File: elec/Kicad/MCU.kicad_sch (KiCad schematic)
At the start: 24 parts, among them J6 SWD, U1 STM32L053C8T6, Y1 32MHz, Y2 32.768KHz

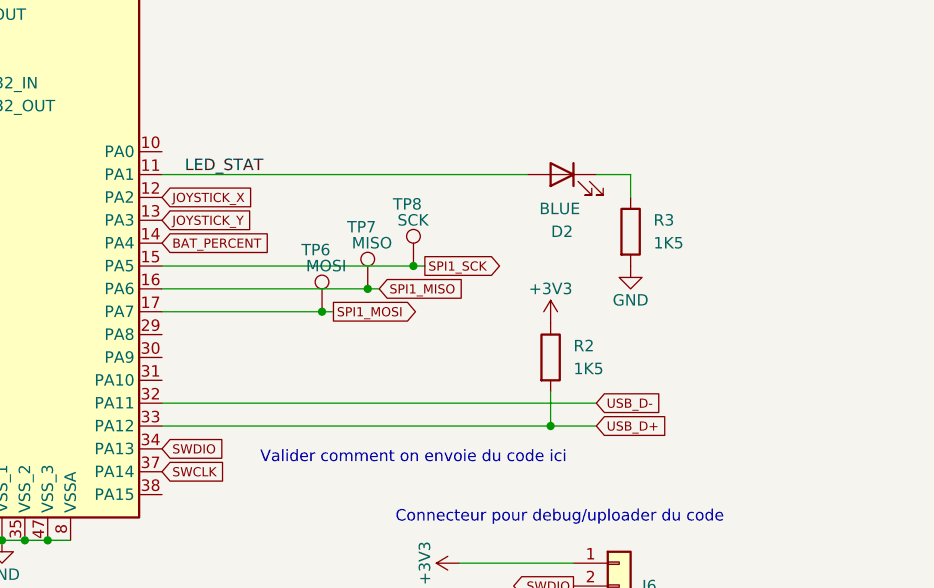
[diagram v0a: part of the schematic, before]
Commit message: add a solder jumper on USB_D+ line in case we need it
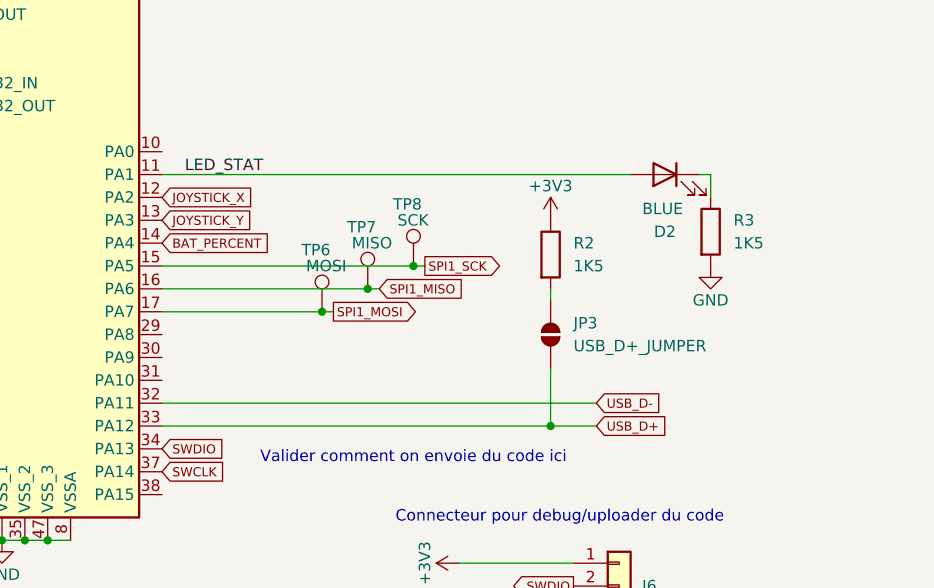
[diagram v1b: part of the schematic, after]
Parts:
- added JP3: USB_D+_JUMPER, symbol Jumper:SolderJumper_2_Open
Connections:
- net USB_D+: now also JP3.1 (A); no longer R2.2
- new net: JP3.2 (B), R2.2
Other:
- moved on the sheet: D2, R2, R3
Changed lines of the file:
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@@
 	(wire
 		(pts
-			(xy 156.21 129.54) (xy 156.21 125.73)
+			(xy 156.21 129.54) (xy 156.21 123.19)
 		)
 		(stroke
@@
 	(wire
 		(pts
-			(xy 161.29 101.6) (xy 165.1 101.6)
+			(xy 172.72 101.6) (xy 173.99 101.6)
 		)
 		(stroke
@@
 	(wire
 		(pts
-			(xy 113.03 101.6) (xy 153.67 101.6)
+			(xy 113.03 101.6) (xy 165.1 101.6)
 		)
 		(stroke
@@
 	(wire
 		(pts
-			(xy 165.1 101.6) (xy 165.1 104.14)
+			(xy 173.99 101.6) (xy 173.99 104.14)
 		)
 		(stroke
@@
 	(wire
 		(pts
+			(xy 156.21 115.57) (xy 156.21 114.3)
+		)
+		(stroke
+			(width 0)
+			(type default)
+		)
+	)
+	(wire
+		(pts
 			(xy 146.05 144.78) (xy 158.75 144.78)
 		)
@@
 	(symbol
 		(lib_id "Device:R")
-		(at 156.21 121.92 0)
+		(at 156.21 110.49 0)
 		(unit 1)
 		(exclude_from_sim no)
@@
 		(fields_autoplaced yes)
 		(property "Reference" "R2"
-			(at 158.75 120.6499 0)
+			(at 158.75 109.2199 0)
 			(effects
 				(font
@@
 		)
 		(property "Value" "1K5"
-			(at 158.75 123.1899 0)
+			(at 158.75 111.7599 0)
 			(effects
 				(font
@@
 		)
 		(property "Footprint" ""
-			(at 154.432 121.92 90)
+			(at 154.432 110.49 90)
 			(effects
 				(font
@@
 		)
 		(property "Datasheet" "https://www.digikey.ca/en/products/detail/vishay-dale/CRCW04021M00FKED/1178349"
-			(at 156.21 121.92 0)
+			(at 156.21 110.49 0)
 			(effects
 				(font
@@
 		)
 		(property "Description" ""
-			(at 156.21 121.92 0)
+			(at 156.21 110.49 0)
 			(effects
 				(font
@@
 	(symbol
 		(lib_id "Device:R")
-		(at 165.1 107.95 0)
+		(at 173.99 107.95 0)
 		(unit 1)
 		(exclude_from_sim no)
@@
 		(fields_autoplaced yes)
 		(property "Reference" "R3"
-			(at 167.64 106.6799 0)
+			(at 176.53 106.6799 0)
 			(effects
 				(font
@@
 		)
 		(property "Value" "1K5"
-			(at 167.64 109.2199 0)
+			(at 176.53 109.2199 0)
 			(effects
 				(font
@@
 		)
 		(property "Footprint" ""
-			(at 163.322 107.95 90)
+			(at 172.212 107.95 90)
 			(effects
 				(font
@@
 		)
 		(property "Datasheet" "https://www.digikey.ca/en/products/detail/yageo/RC0603FR-07510KL/727286"
-			(at 165.1 107.95 0)
+			(at 173.99 107.95 0)
 			(effects
 				(font
@@
 		)
 		(property "Description" ""
-			(at 165.1 107.95 0)
+			(at 173.99 107.95 0)
 			(effects
 				(font
@@
 	(symbol
 		(lib_id "Device:LED")
-		(at 157.48 101.6 0)
+		(at 168.91 101.6 0)
 		(mirror y)
 		(unit 1)
@@
 		(dnp no)
 		(property "Reference" "D2"
-			(at 157.48 107.95 0)
+			(at 168.91 107.95 0)
 			(effects
 				(font
@@
 		)
 		(property "Value" "BLUE"
-			(at 157.226 105.41 0)
+			(at 168.656 105.41 0)
 			(effects
 				(font
@@
 		)
 		(property "Footprint" ""
-			(at 157.48 101.6 0)
+			(at 168.91 101.6 0)
 			(effects
 				(font
@@
 		)
 		(property "Datasheet" "~"
-			(at 157.48 101.6 0)
+			(at 168.91 101.6 0)
 			(effects
 				(font
@@
 		)
 		(property "Description" ""
-			(at 157.48 101.6 0)
+			(at 168.91 101.6 0)
 			(effects
 				(font
@@
 		(lib_name "GND_1")
 		(lib_id "power:GND")
-		(at 165.1 111.76 0)
+		(at 173.99 111.76 0)
 		(unit 1)
 		(exclude_from_sim no)
@@
 		(dnp no)
 		(property "Reference" "#PWR06"
-			(at 165.1 118.11 0)
+			(at 173.99 118.11 0)
 			(effects
 				(font
@@
 		)
 		(property "Value" "GND"
-			(at 165.1 115.57 0)
+			(at 173.99 115.57 0)
 			(effects
 				(font
@@
 		)
 		(property "Footprint" ""
-			(at 165.1 111.76 0)
+			(at 173.99 111.76 0)
 			(effects
 				(font
@@
 		)
 		(property "Datasheet" ""
-			(at 165.1 111.76 0)
+			(at 173.99 111.76 0)
 			(effects
 				(font
@@
 		)
 		(property "Description" "Power symbol creates a global label with name \"GND\" , ground"
-			(at 165.1 111.76 0)
+			(at 173.99 111.76 0)
 			(effects
 				(font
@@
 	)
 	(symbol
+		(lib_id "Jumper:SolderJumper_2_Open")
+		(at 156.21 119.38 90)
+		(unit 1)
+		(exclude_from_sim yes)
+		(in_bom no)
+		(on_board yes)
+		(dnp no)
+		(fields_autoplaced yes)
+		(property "Reference" "JP3"
+			(at 158.75 118.1099 90)
+			(effects
+				(font
+					(size 1.27 1.27)
+				)
+				(justify right)
+			)
+		)
+		(property "Value" "USB_D+_JUMPER"
+			(at 158.75 120.6499 90)
+			(effects
+				(font
+					(size 1.27 1.27)
+				)
+				(justify right)
+			)
+		)
+		(property "Footprint" ""
+			(at 156.21 119.38 0)
+			(effects
+				(font
+					(size 1.27 1.27)
+				)
+				(hide yes)
+			)
+		)
+		(property "Datasheet" "~"
+			(at 156.21 119.38 0)
+			(effects
+				(font
+					(size 1.27 1.27)
+				)
+				(hide yes)
+			)
+		)
+		(property "Description" "Solder Jumper, 2-pole, open"
+			(at 156.21 119.38 0)
+			(effects
+				(font
+					(size 1.27 1.27)
+				)
+				(hide yes)
+			)
+		)
+		(pin "1"
+		)
+		(pin "2"
+		)
+		(instances
+			(project ""
+				(path "/a1545928-1195-40b9-b3c4-78f837012afb/47f0fc71-ff78-496f-bb04-036a9aeaa71c"
+					(reference "JP3")
+					(unit 1)
+				)
+			)
+		)
+	)
+	(symbol
 		(lib_id "Device:R")
 		(at 30.48 55.88 0)
@@
 	(symbol
 		(lib_id "power:+3V3")
-		(at 156.21 118.11 0)
+		(at 156.21 106.68 0)
 		(unit 1)
 		(exclude_from_sim no)
@@
 		(dnp no)
 		(property "Reference" "#PWR04"
-			(at 156.21 121.92 0)
+			(at 156.21 110.49 0)
 			(effects
 				(font
@@
 		)
 		(property "Value" "+3V3"
-			(at 156.21 114.3 0)
+			(at 156.21 102.87 0)
 			(effects
 				(font
@@
 		)
 		(property "Footprint" ""
-			(at 156.21 118.11 0)
+			(at 156.21 106.68 0)
 			(effects
 				(font
@@
 		)
 		(property "Datasheet" ""
-			(at 156.21 118.11 0)
+			(at 156.21 106.68 0)
 			(effects
 				(font
@@
 		)
 		(property "Description" "Power symbol creates a global label with name \"+3V3\""
-			(at 156.21 118.11 0)
+			(at 156.21 106.68 0)
 			(effects
 				(font

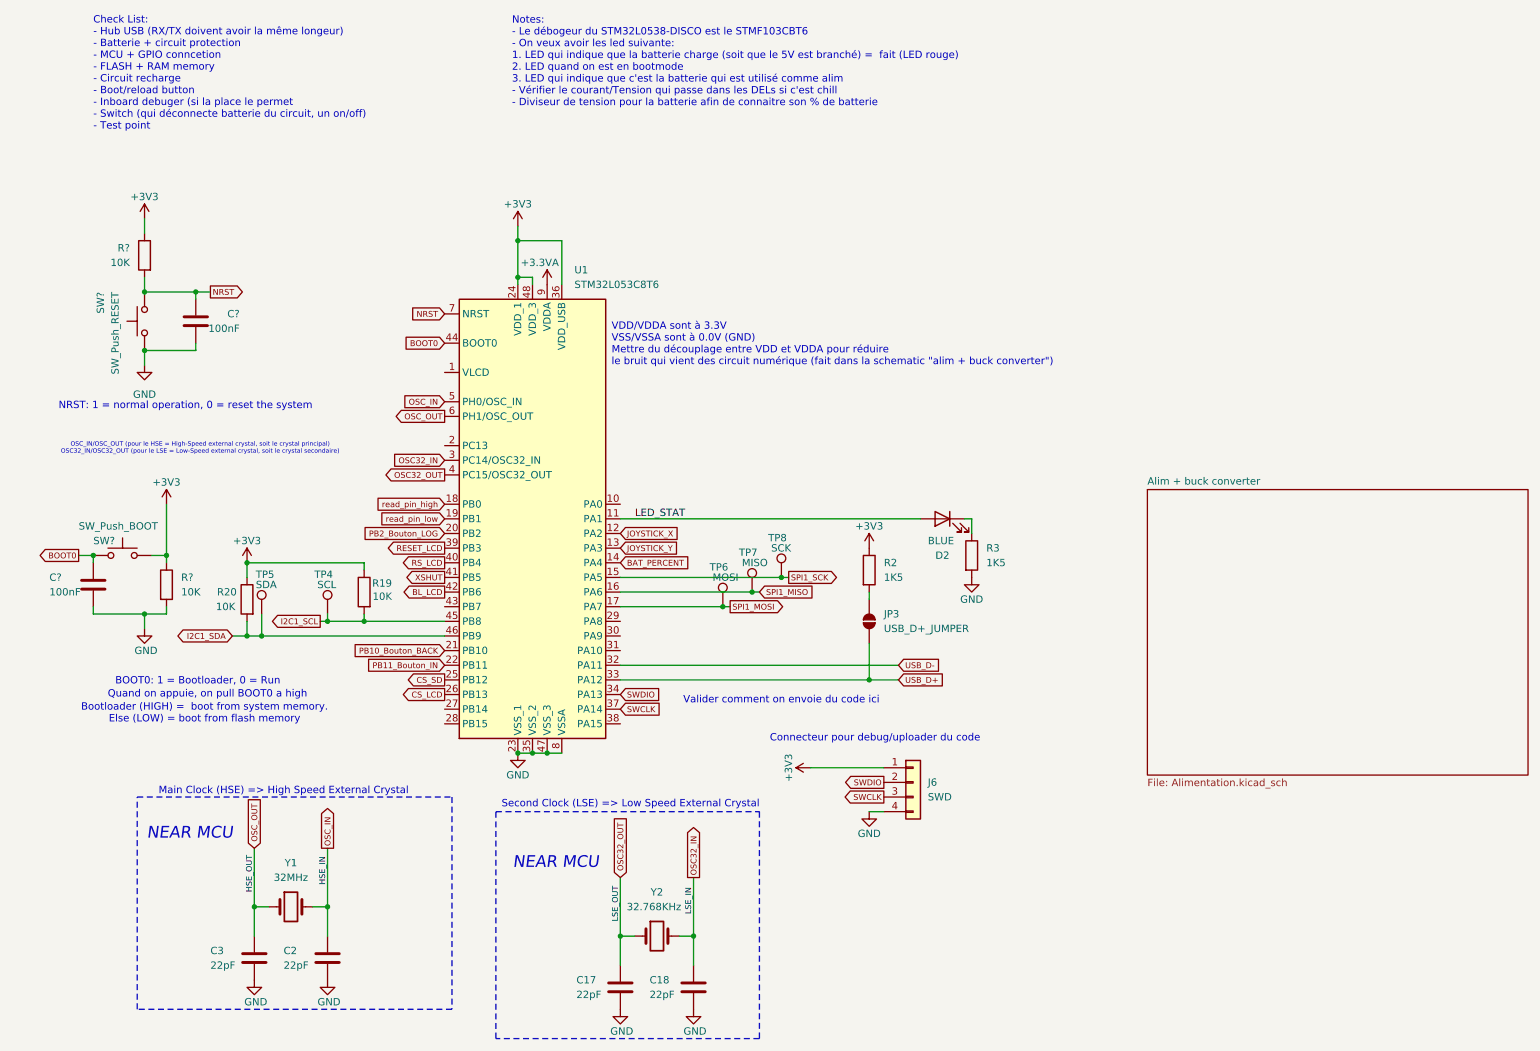
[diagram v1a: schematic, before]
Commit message: add a few footprint
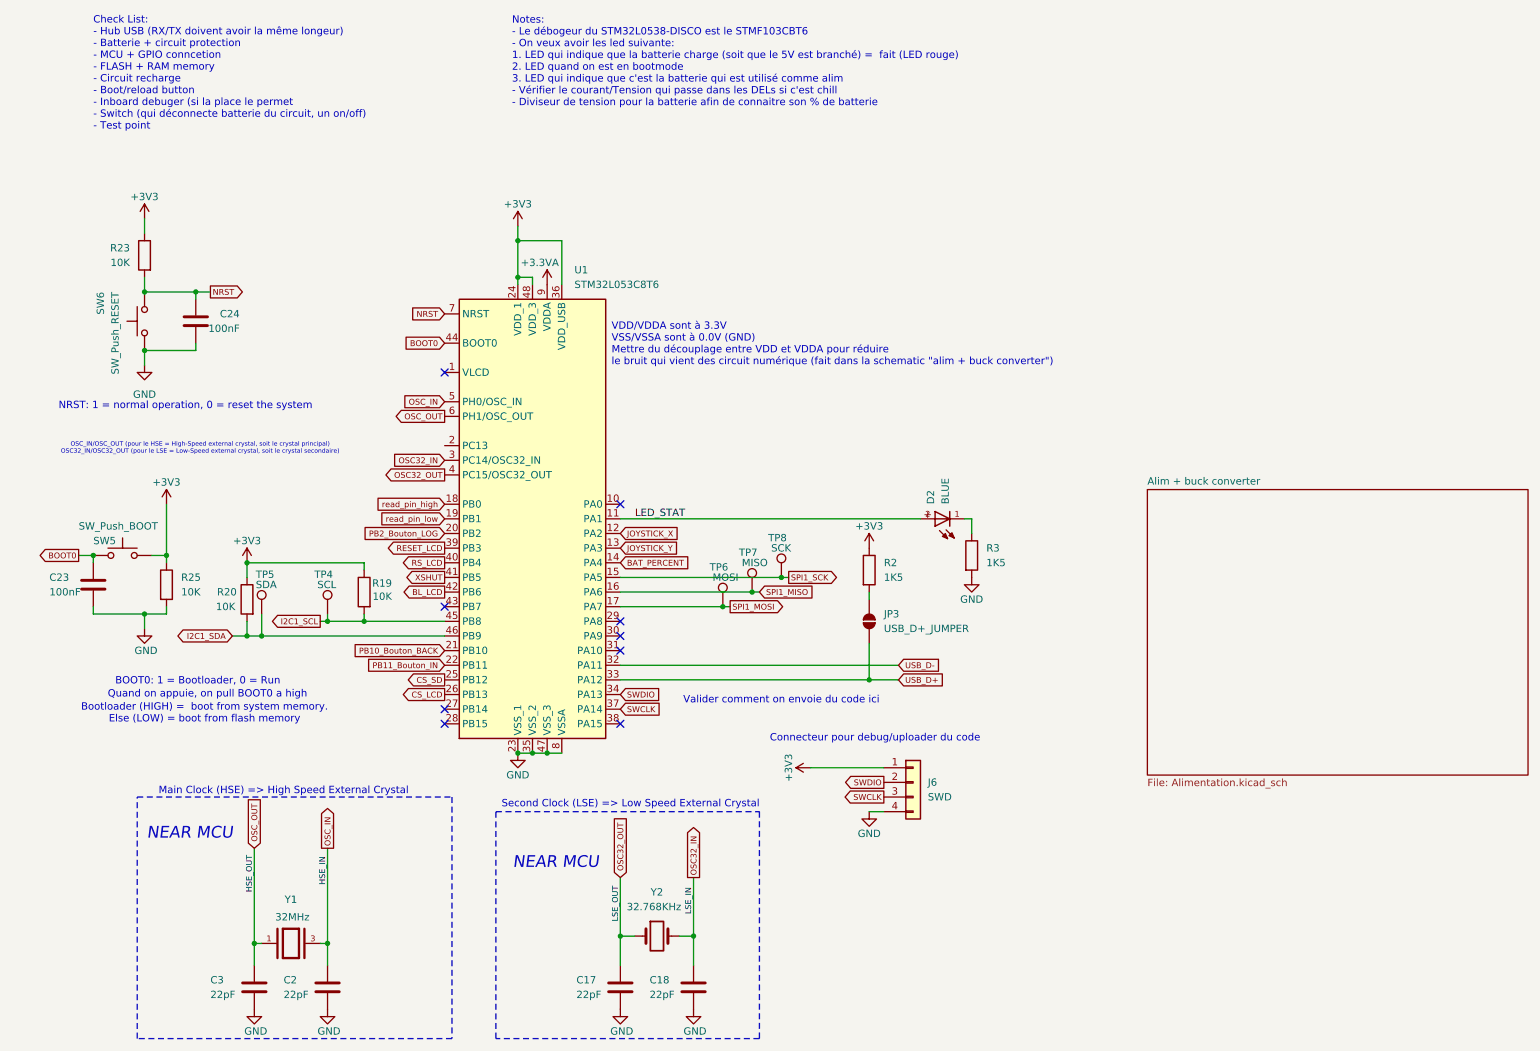
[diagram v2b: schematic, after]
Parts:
- removed D2: BLUE, symbol Device:LED
- removed Y1: 32MHz, symbol Device:Crystal
- added D2: BLUE, SMD_LED_0603:WL-SMCD_0603, symbol WL-SMCD_0603:WL-SMCD_0603
- added Y1: 32MHz, XRCGB32M000F2P01R0:OSC_XRCGB32M000F2P01R0, symbol XRCGB32M000F2P01R0:XRCGB32M000F2P01R0
- C17, C18, C2, C3: footprint (none) -> Capacitor_SMD:C_0603_1608Metric_Pad1.08x0.95mm_HandSolder
- C23, C24: renamed from C?; footprint (none) -> Capacitor_SMD:C_0603_1608Metric_Pad1.08x0.95mm_HandSolder
- J6: footprint Connector_PinHeader_1.00mm:PinHeader_1x04_P1.00mm_Vertical -> Connector_PinHeader_2.54mm:PinHeader_1x04_P2.54mm_Vertical
- JP3: footprint (none) -> Jumper:SolderJumper-2_P1.3mm_Open_TrianglePad1.0x1.5mm
- R19, R2, R20, R3: footprint (none) -> Resistor_SMD:R_0603_1608Metric_Pad0.98x0.95mm_HandSolder
- R23, R25: renamed from R?; footprint (none) -> Resistor_SMD:R_0603_1608Metric_Pad0.98x0.95mm_HandSolder
- SW5, SW6: renamed from SW?; footprint (none) -> Button_Switch_SMD:SW_SPST_PTS647_Sx38
- TP4, TP5, TP6, TP7, TP8: footprint (none) -> TestPoint:TestPoint_Loop_D1.80mm_Drill1.0mm_Beaded
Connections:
- net LED_STAT: now also D2.2
- net OSC_IN: now also Y1.3
- net OSC_OUT: now also Y1.1
- net at R3.1: now also D2.1
- no-connect marks 0 -> 9
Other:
- moved on the sheet: C2, C3

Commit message: formation torture
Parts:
- added J1: SWD, Connector_PinHeader_2.54mm:PinHeader_1x04_P2.54mm_Vertical, symbol Connector_Generic:Conn_01x04
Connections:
- net +3V3: now also J1.1 (Pin_1); no longer R19.1, R2.1, R20.1, R23.1, R25.1, SW5.1, U1.24 (VDD_1), U1.36 (VDD_USB), U1.48 (VDD_3)
- net GND: now also J1.4 (Pin_4)
- net USART1_TX: now reaches U1.30 (PA9)
- net USART1_TX: now also J1.2 (Pin_2)
- net USART1_RX: now reaches U1.31 (PA10)
- net USART1_RX: now also J1.3 (Pin_3)
- new net +3.3V: R19.1, R2.1, R20.1, R23.1, R25.1, SW5.1, U1.24 (VDD_1), U1.36 (VDD_USB), U1.48 (VDD_3)
- no-connect marks 9 -> 8
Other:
- note added: "Connector"
- note added: "USART Connector"
- moved on the sheet: J6, JP3, R2

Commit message: J'ai ajouter des power Flag pour spécifier a Kicad que c'est chill (faut qu'il apprenne a ce géré quand même)
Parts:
- removed JP3: USB_D+_JUMPER, Jumper:SolderJumper-2_P1.3mm_Open_TrianglePad1.0x1.5mm, symbol Jumper:SolderJumper_2_Open
- removed R2: 1K5, Resistor_SMD:R_0603_1608Metric_Pad0.98x0.95mm_HandSolder, symbol Device:R

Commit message: ajout d'un Mosfet de type N pour pouvoir gérer le % de batterie (ADC)
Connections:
- net +3V3 is gone; now on net +3.3V: J1.1 (Pin_1), J6.1 (Pin_1)
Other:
- note added: "Check List: - Hub USB (RX/TX doivent avoir la même longeur) - MCU + GPIO conncetion - Test point"
- note added: "HSE_IN"
- note added: "HSE_OUT"
- note added: "LSE_IN"
- note added: "LSE_OUT"
- note added: "Notes: Finir la schematic de charles"
- note removed: "Check List: - Hub USB (RX/TX doivent avoir la même longeur) - Batterie + circuit protection - MCU + GPIO conncetion - FLASH + RAM memory - Circuit recharge - Boot/reload button - Inboard debuger (si la place le permet - Switch (qui déconnecte batterie du circuit, un on/off) - Test point"
- note removed: "Notes: - Le débogeur du STM32L0538-DISCO est le STMF103CBT6 - On veux avoir les led suivante: 1. LED qui indique que la batterie charge (soit que le 5V est branché) = fait (LED rouge) 2. LED quand on est en bootmode 3. LED qui indique que c'est la batterie qui est utilisé comme alim - Vérifier le courant/Tension qui passe dans les DELs si c'est chill - Diviseur de tension pour la batterie afin de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"

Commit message: commencer le PCB vite fait
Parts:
- removed TP4: SCL, TestPoint:TestPoint_Loop_D1.80mm_Drill1.0mm_Beaded, symbol Connector:TestPoint
- removed TP5: SDA, TestPoint:TestPoint_Loop_D1.80mm_Drill1.0mm_Beaded, symbol Connector:TestPoint
- removed TP6: MOSI, TestPoint:TestPoint_Loop_D1.80mm_Drill1.0mm_Beaded, symbol Connector:TestPoint
- removed TP7: MISO, TestPoint:TestPoint_Loop_D1.80mm_Drill1.0mm_Beaded, symbol Connector:TestPoint
- removed TP8: SCK, TestPoint:TestPoint_Loop_D1.80mm_Drill1.0mm_Beaded, symbol Connector:TestPoint
- added J5: TestPoint, Connector_PinSocket_2.54mm:PinSocket_1x10_P2.54mm_Vertical, symbol Connector_Generic:Conn_01x10
- J1: value SWD -> USART
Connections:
- net +3.3V: now also J5.2 (Pin_2)
- net BAT_PERCENT: now also J5.4 (Pin_4)
- net GND: now also J5.10 (Pin_10)
- net I2C1_SCL: now also J5.5 (Pin_5)
- net I2C1_SDA: now also J5.6 (Pin_6)
- net SPI1_MISO: now also J5.8 (Pin_8)
- net SPI1_MOSI: now also J5.9 (Pin_9)
- net SPI1_SCK: now also J5.7 (Pin_7)
- new net +2V8: J5.1 (Pin_1)
- new net +5V: J5.3 (Pin_3)

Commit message: touillerie
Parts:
- removed J1: USART, Connector_PinHeader_2.54mm:PinHeader_1x04_P2.54mm_Vertical, symbol Connector_Generic:Conn_01x04
- removed J6: SWD, Connector_PinHeader_2.54mm:PinHeader_1x04_P2.54mm_Vertical, symbol Connector_Generic:Conn_01x04
- removed SW5: SW_Push_BOOT, Button_Switch_SMD:SW_SPST_PTS647_Sx38, symbol Switch:SW_Push
- removed SW6: SW_Push_RESET, Button_Switch_SMD:SW_SPST_PTS647_Sx38, symbol Switch:SW_Push
- added J1: USART, Connector_PinHeader_2.54mm:PinHeader_1x02_P2.54mm_Vertical, symbol Connector_Generic:Conn_01x02
- added J6: SWD, Connector_PinHeader_2.54mm:PinHeader_1x02_P2.54mm_Vertical, symbol Connector_Generic:Conn_01x02
- added SW4: SW_Push_RESET, B3U_1100P:B3U-1100P_OMR, symbol B3U_1100P:B3U-1100P
- added SW5: SW_Push_BOOT, B3U_1100P:B3U-1100P_OMR, symbol B3U_1100P:B3U-1100P
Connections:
- net +3.3V: now also SW5.2
- net BOOT0: now also SW5.1
- net GND: now also SW4.2
- net NRST: now also SW4.1
- net SWCLK: now also J6.2 (Pin_2)
- net SWDIO: now also J6.1 (Pin_1)
- net USART1_RX: now also J1.2 (Pin_2)
- net USART1_TX: now also J1.1 (Pin_1)
- net read_pin_high renamed read_pin
- net read_pin_low: no longer names the net of U1.19 (PB1)
- no-connect marks 8 -> 11
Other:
- note removed: "Notes: Finir la schematic de charles"
- note removed: "Valider comment on envoie du code ici"
- moved on the sheet: C24, R23
